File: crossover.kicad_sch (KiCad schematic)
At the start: 7 parts, among them J1 Power In, J2 Line In, J3 Tweeter Out, J4 Sub Out, U6 TL072

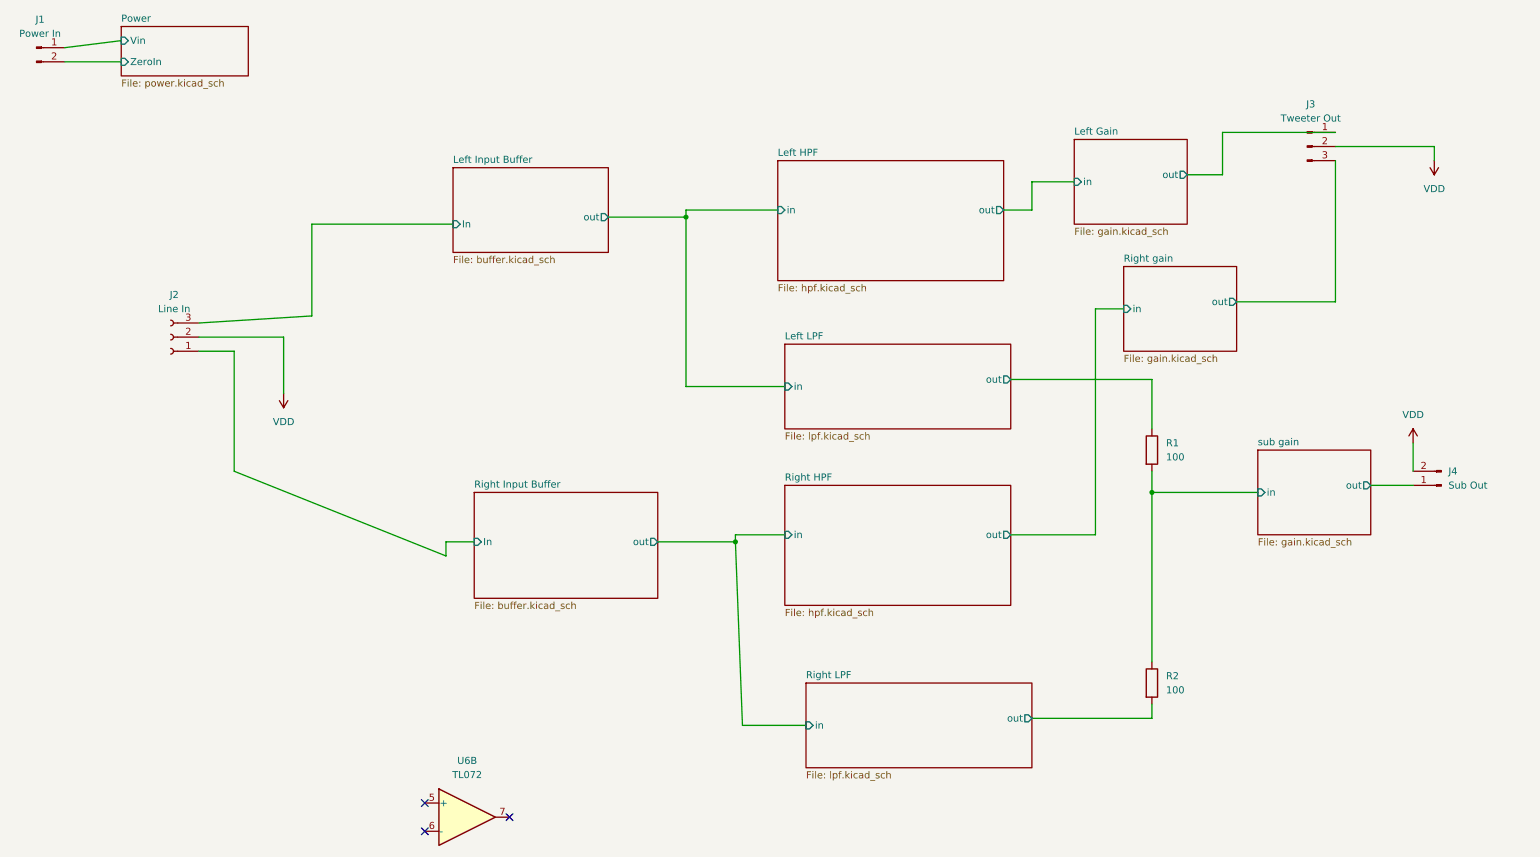
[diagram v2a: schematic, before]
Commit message: Allow stereo/mono switching for Sub
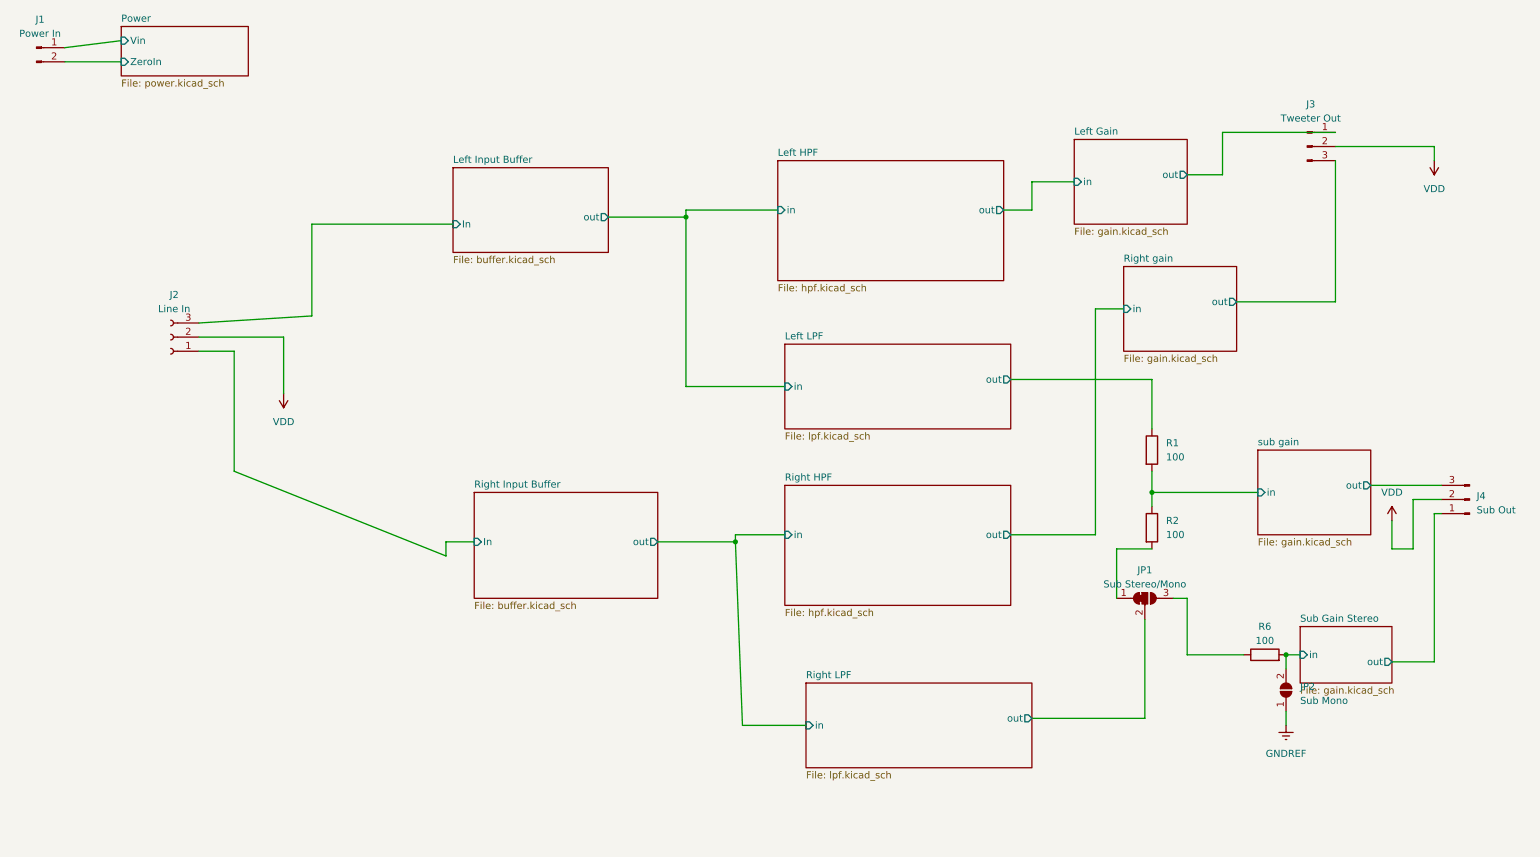
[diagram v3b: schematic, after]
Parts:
- removed J4: Sub Out, Connector_JST:JST_EH_B2B-EH-A_1x02_P2.50mm_Vertical, symbol Connector:Conn_01x02_Male
- removed U6: TL072, Package_DIP:DIP-8_W7.62mm_Socket, symbol Amplifier_Operational:TL072
- added J4: Sub Out, Connector_JST:JST_EH_B3B-EH-A_1x03_P2.50mm_Vertical, symbol Connector:Conn_01x03_Male
- added JP1: Sub Stereo/Mono, symbol Jumper:SolderJumper_3_Bridged12
- added JP2: Sub Mono, symbol Jumper:SolderJumper_2_Open
- added R6: 100, Resistor_THT:R_Axial_DIN0207_L6.3mm_D2.5mm_P7.62mm_Horizontal, symbol Device:R
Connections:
- net Right LPF/out: now also JP1.2 (C); no longer R2.2
- net VDD: now also J4.2 (Pin_2)
- net sub gain/out: now also J4.3 (Pin_3)
- new net: JP1.3 (B), R6.1
- new net: JP1.1 (A), R2.2
- new net GNDREF: JP2.1 (A)
- new net Sub Gain Stereo/in: JP2.2 (B), R6.2
- new net Sub Gain Stereo/out: J4.1 (Pin_1)
- no-connect marks 3 -> 0
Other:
- added sheet Sub Gain Stereo (gain.kicad_sch)
- moved on the sheet: R2

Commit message: Re-annotate and run erc
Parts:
- renumbered R6 to R3
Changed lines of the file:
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@@
   (symbol (lib_id "power:VDD") (at 264.16 118.11 0) (unit 1)
     (in_bom yes) (on_board yes) (dnp no) (fields_autoplaced)
-    (property "Reference" "#PWR02" (at 264.16 121.92 0)
+    (property "Reference" "#PWR03" (at 264.16 121.92 0)
       (effects (font (size 1.27 1.27)) hide)
     )
@@
       (project "crossover"
         (path "/3c8df2a5-e9f9-4495-af40-aa221f0b3fa5"
-          (reference "#PWR02") (unit 1)
+          (reference "#PWR03") (unit 1)
         )
       )
@@
   (symbol (lib_id "power:GNDREF") (at 245.11 154.94 0) (unit 1)
     (in_bom yes) (on_board yes) (dnp no) (fields_autoplaced)
-    (property "Reference" "#PWR036" (at 245.11 161.29 0)
+    (property "Reference" "#PWR02" (at 245.11 161.29 0)
       (effects (font (size 1.27 1.27)) hide)
     )
@@
       (project "crossover"
         (path "/3c8df2a5-e9f9-4495-af40-aa221f0b3fa5"
-          (reference "#PWR036") (unit 1)
+          (reference "#PWR02") (unit 1)
         )
       )
@@
   (symbol (lib_id "Device:R") (at 241.3 142.24 90) (unit 1)
     (in_bom yes) (on_board yes) (dnp no) (fields_autoplaced)
-    (property "Reference" "R6" (at 241.3 137.16 90)
+    (property "Reference" "R3" (at 241.3 137.16 90)
       (effects (font (size 1.27 1.27)))
     )
@@
       (project "crossover"
         (path "/3c8df2a5-e9f9-4495-af40-aa221f0b3fa5"
-          (reference "R6") (unit 1)
+          (reference "R3") (unit 1)
         )
       )
@@
   (symbol (lib_id "power:VDD") (at 271.78 53.34 180) (unit 1)
     (in_bom yes) (on_board yes) (dnp no) (fields_autoplaced)
-    (property "Reference" "#PWR03" (at 271.78 49.53 0)
+    (property "Reference" "#PWR04" (at 271.78 49.53 0)
       (effects (font (size 1.27 1.27)) hide)
     )
@@
       (project "crossover"
         (path "/3c8df2a5-e9f9-4495-af40-aa221f0b3fa5"
-          (reference "#PWR03") (unit 1)
-        )
-      )
+          (reference "#PWR04") (unit 1)
+        )
+      )

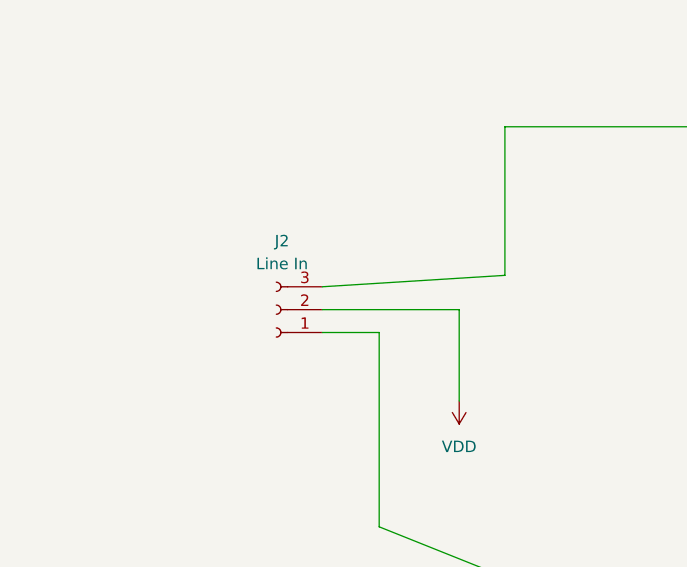
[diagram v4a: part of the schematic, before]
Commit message: Fix some ERC warnings
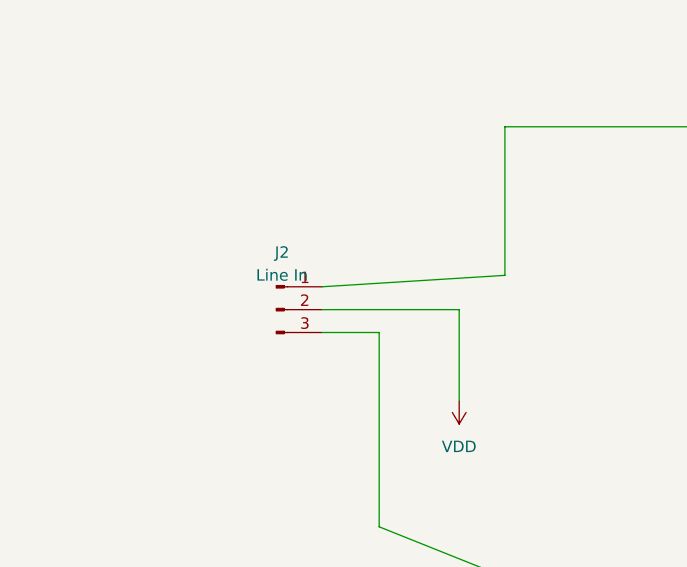
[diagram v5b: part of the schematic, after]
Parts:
- removed J4: Sub Out, Connector_JST:JST_EH_B3B-EH-A_1x03_P2.50mm_Vertical, symbol Connector:Conn_01x03_Male
- added J4: Sub Out, symbol Connector:Conn_01x03_Pin
- J1: symbol Connector:Conn_01x02_Male -> Connector:Conn_01x02_Pin
- J2: symbol Connector:Conn_01x03_Female -> Connector:Conn_01x03_Pin
- J3: symbol Connector:Conn_01x03_Male -> Connector:Conn_01x03_Pin
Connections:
- net Left Input Buffer/In: now also J2.1 (Pin_1); no longer J2.3 (Pin_3)
- net Right Input Buffer/In: now also J2.3 (Pin_3); no longer J2.1 (Pin_1)
- net Sub Gain Stereo/out: now also J4.1 (Pin_1)
- net VDD: now also J4.2 (Pin_2)
- net sub gain/out: now also J4.3 (Pin_3)

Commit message: Assign footprints to everything
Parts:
- J4: footprint (none) -> Connector_JST:JST_EH_B3B-EH-A_1x03_P2.50mm_Vertical
- JP1: footprint (none) -> Jumper:SolderJumper-3_P1.3mm_Open_RoundedPad1.0x1.5mm
- JP2: footprint (none) -> Jumper:SolderJumper-2_P1.3mm_Open_RoundedPad1.0x1.5mm
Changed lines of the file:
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@@
       (effects (font (size 1.27 1.27)) (justify right))
     )
-    (property "Footprint" "" (at 245.11 148.59 0)
+    (property "Footprint" "Jumper:SolderJumper-2_P1.3mm_Open_RoundedPad1.0x1.5mm" (at 245.11 148.59 0)
       (effects (font (size 1.27 1.27)) hide)
     )
@@
       (effects (font (size 1.27 1.27)))
     )
-    (property "Footprint" "" (at 219.71 132.08 0)
+    (property "Footprint" "Jumper:SolderJumper-3_P1.3mm_Open_RoundedPad1.0x1.5mm" (at 219.71 132.08 0)
       (effects (font (size 1.27 1.27)) hide)
     )
@@
       (effects (font (size 1.27 1.27)) (justify right))
     )
-    (property "Footprint" "" (at 278.13 114.3 0)
-      (effects (font (size 1.27 1.27)) hide)
-    )
+    (property "Footprint" "Connector_JST:JST_EH_B3B-EH-A_1x03_P2.50mm_Vertical" (at 278.13 114.3 0)
+      (effects (font (size 1.27 1.27)) hide)
+    )

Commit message: Finish placing
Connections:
- net Left Input Buffer/In: now also J2.3 (Pin_3); no longer J2.1 (Pin_1)
- net Right Input Buffer/In: now also J2.1 (Pin_1); no longer J2.3 (Pin_3)
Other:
- moved on the sheet: J2
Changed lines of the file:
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@@
+    (stroke (width 0) (type default))
+  )
+  (wire (pts (xy 64.77 87.63) (xy 69.85 87.63))
     (stroke (width 0) (type default))
   )
@@
     (stroke (width 0) (type default))
   )
-  (wire (pts (xy 64.77 85.09) (xy 64.77 95.25))
-    (stroke (width 0) (type default))
-  )
   (wire (pts (xy 95.25 64.77) (xy 69.85 64.77))
     (stroke (width 0) (type default))
   )
   (wire (pts (xy 93.98 121.92) (xy 99.06 121.92))
+    (stroke (width 0) (type default))
+  )
+  (wire (pts (xy 55.88 87.63) (xy 59.69 87.63))
     (stroke (width 0) (type default))
   )
@@
     (stroke (width 0) (type default))
   )
-  (wire (pts (xy 210.82 120.65) (xy 210.82 80.01))
+  (wire (pts (xy 69.85 64.77) (xy 69.85 85.09))
     (stroke (width 0) (type default))
   )
-  (wire (pts (xy 49.53 85.09) (xy 64.77 85.09))
+  (wire (pts (xy 210.82 120.65) (xy 210.82 80.01))
     (stroke (width 0) (type default))
   )
@@
   )
   (wire (pts (xy 93.98 124.46) (xy 93.98 121.92))
+    (stroke (width 0) (type default))
+  )
+  (wire (pts (xy 59.69 90.17) (xy 69.85 90.17))
+    (stroke (width 0) (type default))
+  )
+  (wire (pts (xy 64.77 95.25) (xy 64.77 87.63))
     (stroke (width 0) (type default))
   )
@@
   )
   (wire (pts (xy 220.98 113.03) (xy 220.98 109.22))
-    (stroke (width 0) (type default))
-  )
-  (wire (pts (xy 69.85 64.77) (xy 69.85 81.28))
     (stroke (width 0) (type default))
   )
@@
     (stroke (width 0) (type default))
   )
-  (wire (pts (xy 49.53 87.63) (xy 55.88 87.63))
-    (stroke (width 0) (type default))
-  )
   (wire (pts (xy 137.16 63.5) (xy 137.16 62.23))
     (stroke (width 0) (type default))
@@
   )
   (wire (pts (xy 267.97 114.3) (xy 273.05 114.3))
+    (stroke (width 0) (type default))
+  )
+  (wire (pts (xy 59.69 87.63) (xy 59.69 90.17))
     (stroke (width 0) (type default))
   )
@@
     (stroke (width 0) (type default))
   )
-  (wire (pts (xy 69.85 81.28) (xy 49.53 82.55))
-    (stroke (width 0) (type default))
-  )
   (wire (pts (xy 199.39 153.67) (xy 219.71 153.67))
     (stroke (width 0) (type default))
@@
     (stroke (width 0) (type default))
   )
-  (symbol (lib_id "Connector:Conn_01x03_Pin") (at 44.45 85.09 0) (unit 1)
+  (symbol (lib_id "Connector:Conn_01x03_Pin") (at 74.93 87.63 180) (unit 1)
     (in_bom yes) (on_board yes) (dnp no) (fields_autoplaced)
-    (property "Reference" "J2" (at 45.085 78.74 0)
-      (effects (font (size 1.27 1.27)))
+    (property "Reference" "J2" (at 76.2 86.995 0)
+      (effects (font (size 1.27 1.27)) (justify right))
     )
-    (property "Value" "Line In" (at 45.085 81.28 0)
-      (effects (font (size 1.27 1.27)))
+    (property "Value" "Line In" (at 76.2 89.535 0)
+      (effects (font (size 1.27 1.27)) (justify right))
     )
-    (property "Footprint" "Connector_JST:JST_EH_B3B-EH-A_1x03_P2.50mm_Vertical" (at 44.45 85.09 0)
+    (property "Footprint" "Connector_JST:JST_EH_B3B-EH-A_1x03_P2.50mm_Vertical" (at 74.93 87.63 0)
       (effects (font (size 1.27 1.27)) hide)
     )
-    (property "Datasheet" "~" (at 44.45 85.09 0)
+    (property "Datasheet" "~" (at 74.93 87.63 0)
       (effects (font (size 1.27 1.27)) hide)
     )
